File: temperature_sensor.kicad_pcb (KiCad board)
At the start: 2 copper layers, 8 parts, among them U3 XIAO-SAMD21-SMD, U4 AD589MH, U5 TMP37FT9Z

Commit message: i need to revert some of this to get my old stuff back lol
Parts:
- removed R10: 182k, Resistor_SMD:R_1210_3225Metric_Pad1.30x2.65mm_HandSolder
- removed R7: 45.3k, Resistor_SMD:R_1210_3225Metric_Pad1.30x2.65mm_HandSolder
- removed R8, R9: 10k, Resistor_SMD:R_1210_3225Metric_Pad1.30x2.65mm_HandSolder
- removed U4: AD589MH, 1_my_custom_library:AD589MH
- moved U5 25.7 mm to (68.3, 39.7)
- moved RF_interceptor1 17.4 mm to (66.9, 45.5)
- moved U3 5.62 mm to (45.0, 60.9)
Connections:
- U3 pad 2: unconnected-(U3-PA4_A1_D1-Pad2) -> Net-(U3-PA4_A1_D1)
- U5 pad 2: Net-(U5-VOUT) -> Net-(U3-PA4_A1_D1)
- U5 pad 3: Net-(U4-V-) -> GND

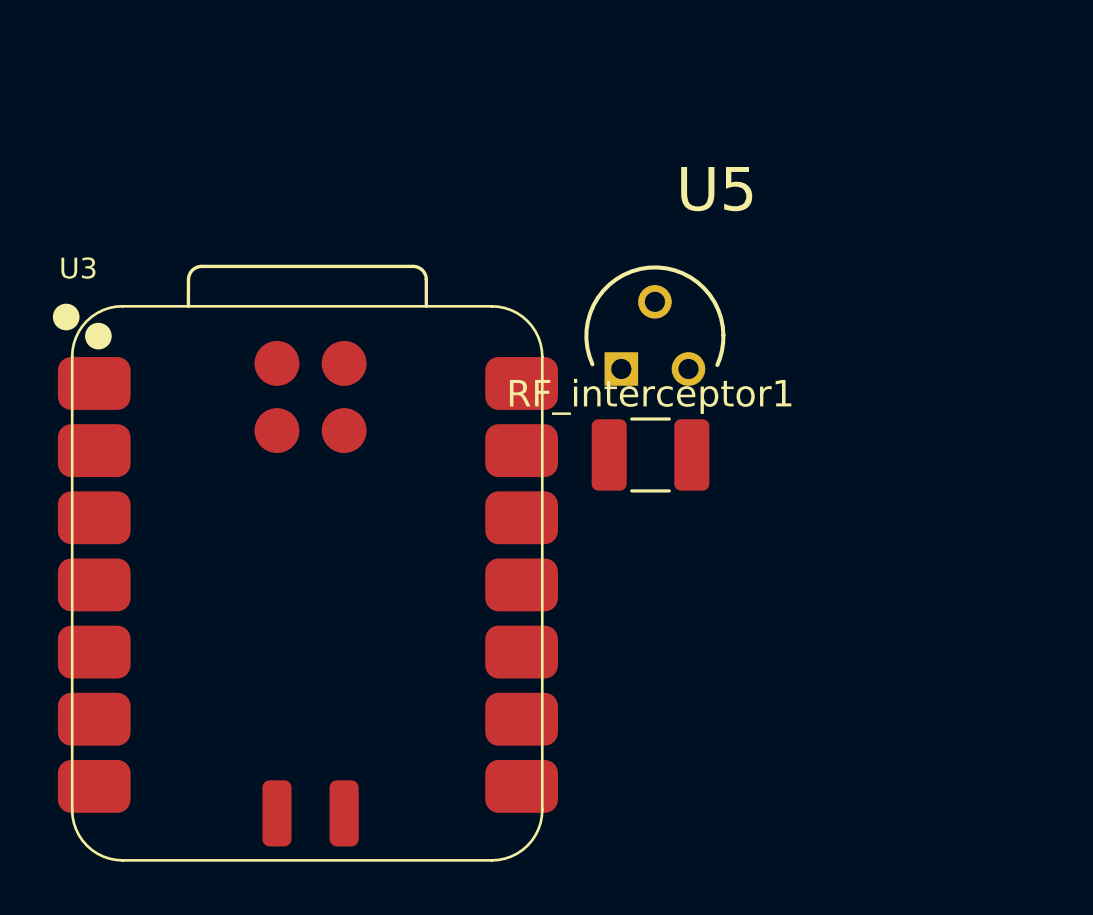
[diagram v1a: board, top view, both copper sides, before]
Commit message: added potentiometer, photoresistor, switch between the two and off, and added a F/C switch. need to up current into LCD's A pin
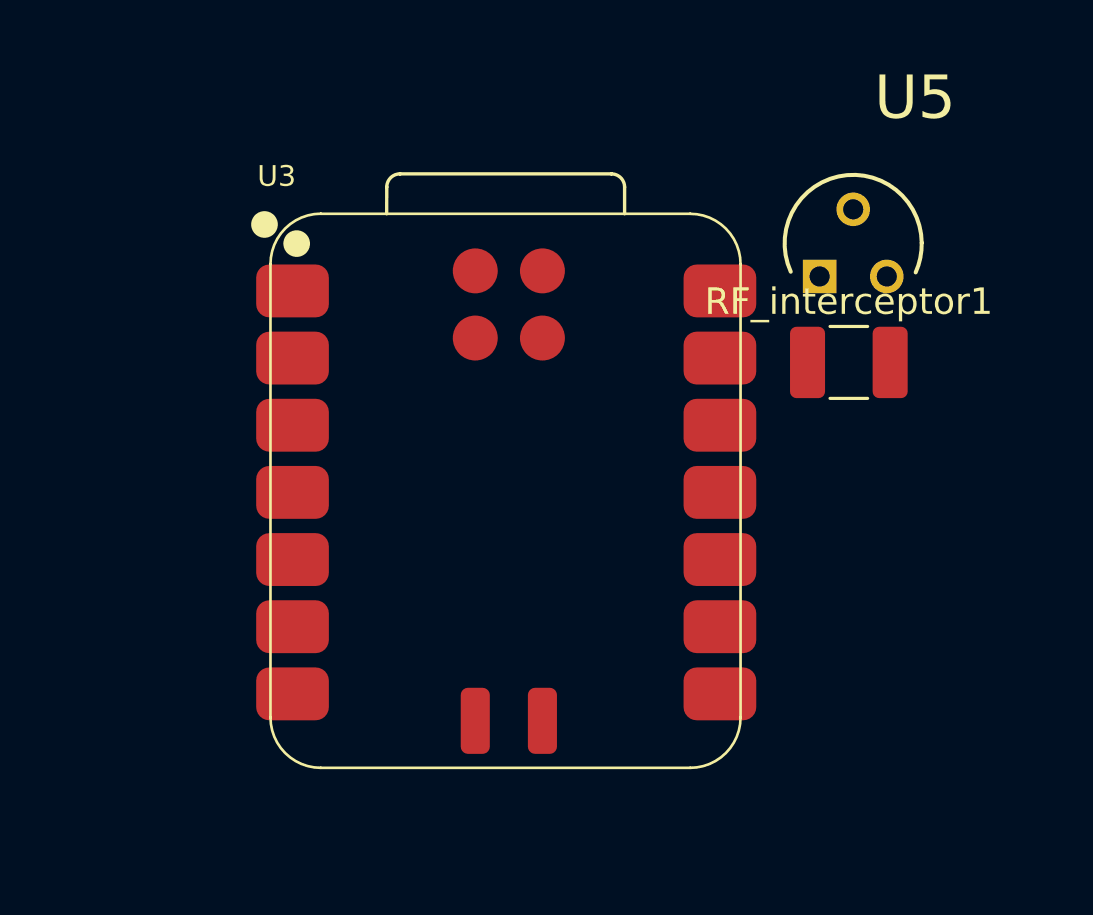
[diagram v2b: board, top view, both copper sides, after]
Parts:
- moved RF_interceptor1 8.28 mm to (74.4, 42.0)
- moved U3 8.28 mm to (52.5, 57.4)
- moved U5 8.28 mm to (75.8, 36.2)
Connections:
- net Net-(U3-3V3) renamed /3v3
- U3 pad 3: unconnected-(U3-PA10_A2_D2-Pad3) -> Net-(DS1-~{CS1})
- U3 pad 4: unconnected-(U3-PA11_A3_D3-Pad4) -> Net-(DS1-~{RES})
- U3 pad 5: unconnected-(U3-PA8_A4_D4_SDA-Pad5) -> Net-(DS1-A0)

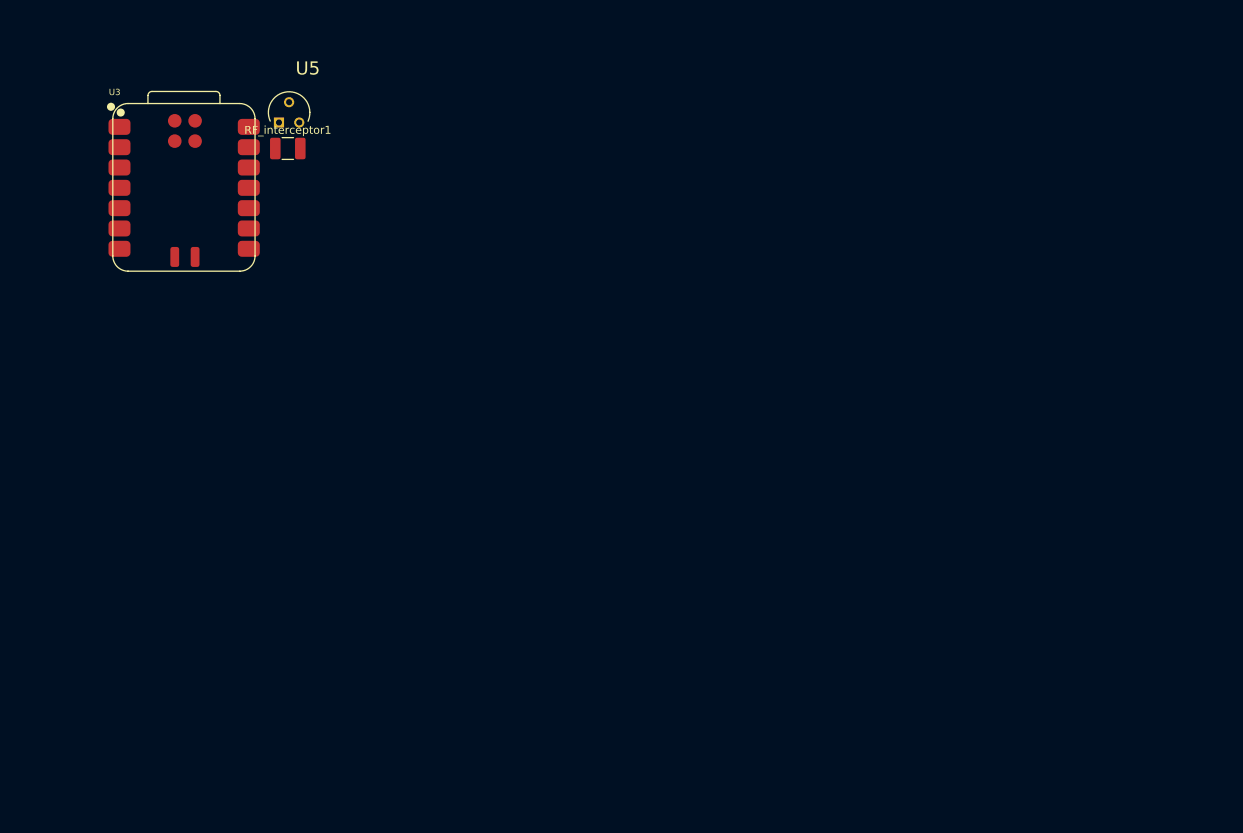
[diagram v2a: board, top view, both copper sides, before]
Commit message: got everything except the MOSFET to step up the current to 80mA.  all footprints added
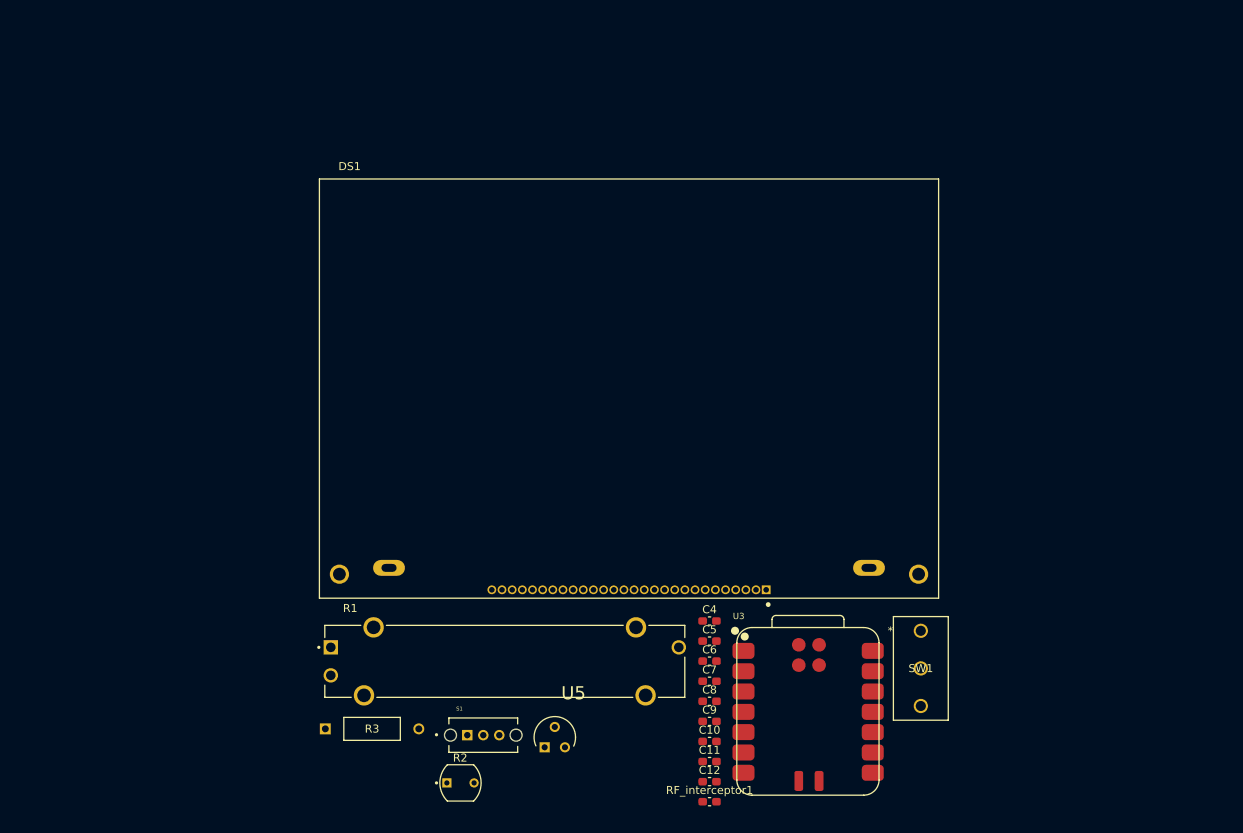
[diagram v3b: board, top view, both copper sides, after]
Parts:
- added C10: 1u, Capacitor_SMD:C_0603_1608Metric_Pad1.08x0.95mm_HandSolder, F.Cu at (127.1, 116.1)
- added C11: 1u, Capacitor_SMD:C_0603_1608Metric_Pad1.08x0.95mm_HandSolder, F.Cu at (127.1, 118.6)
- added C12: 1u, Capacitor_SMD:C_0603_1608Metric_Pad1.08x0.95mm_HandSolder, F.Cu at (127.1, 121.1)
- added C4: 2.2u, Capacitor_SMD:C_0603_1608Metric_Pad1.08x0.95mm_HandSolder, F.Cu at (127.1, 101.0)
- added C5: 2.2u, Capacitor_SMD:C_0603_1608Metric_Pad1.08x0.95mm_HandSolder, F.Cu at (127.1, 103.5)
- added C6: 2.2u, Capacitor_SMD:C_0603_1608Metric_Pad1.08x0.95mm_HandSolder, F.Cu at (127.1, 106.0)
- added C7: 2.2u, Capacitor_SMD:C_0603_1608Metric_Pad1.08x0.95mm_HandSolder, F.Cu at (127.1, 108.6)
- added C8: 2.2u, Capacitor_SMD:C_0603_1608Metric_Pad1.08x0.95mm_HandSolder, F.Cu at (127.1, 111.1)
- added C9: 1u, Capacitor_SMD:C_0603_1608Metric_Pad1.08x0.95mm_HandSolder, F.Cu at (127.1, 113.6)
- added DS1: NHD-C12864LZ-FSW-FBW-3V3, 1_my_custom_library:LCD_NHD-C12864LZ-FSW-FBW-3V3, F.Cu at (117.0, 98.2)
- added R1: PTA3043-2010CIB103, 1_my_custom_library:slide_potentiometer, F.Cu at (101.5, 106.1)
- added R2: PDV-P8103, 1_my_custom_library:photoresistor, F.Cu at (96.0, 121.3)
- added R3: 10k, 1_my_custom_library:YAG_MF25_YAG, F.Cu at (79.1, 114.5)
- added S1: OS102011MS2QN1, 1_my_custom_library:slideSwitch, F.Cu at (98.8, 115.3)
- added SW1: 500SSP3S1M2QEA, 1_my_custom_library:onOffOn, F.Cu at (153.5, 102.2)
- RF_interceptor1: footprint Capacitor_SMD:C_1210_3225Metric_Pad1.33x2.70mm_HandSolder -> Capacitor_SMD:C_0603_1608Metric_Pad1.08x0.95mm_HandSolder
- moved U3 101.9 mm to (130.5, 122.9)
- moved RF_interceptor1 97.2 mm to (127.1, 123.6)
- moved U5 84.9 mm to (109.0, 114.3)
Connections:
- net /3v3 renamed Net-(DS1-C86)
- U3 pad 1: unconnected-(U3-PA02_A0_D0-Pad1) -> Net-(U3-PA02_A0_D0)
- U3 pad 10: unconnected-(U3-PA5_A9_D9_MISO-Pad10) -> Net-(U3-PA5_A9_D9_MISO)
- U3 pad 13: unconnected-(U3-GND-Pad13) -> GND
- U3 pad 6: unconnected-(U3-PA9_A5_D5_SCL-Pad6) -> Net-(DS1-DB6)
- U3 pad 7: unconnected-(U3-PB08_A6_D6_TX-Pad7) -> Net-(DS1-A0)
- U3 pad 8: unconnected-(U3-PB09_A7_D7_RX-Pad8) -> Net-(DS1-~{WR}/R/W)
- U3 pad 9: unconnected-(U3-PA7_A8_D8_SCK-Pad9) -> Net-(U3-PA7_A8_D8_SCK)

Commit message: initial pcb design
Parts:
- added R4: 820, 1_my_custom_library:RESC6332X65N, F.Cu at (128.9, 87.5)
- added TP1: gnd_TP, Connector_Pin:Pin_D1.0mm_L10.0mm, F.Cu at (49.0, 112.0)
- added TP2: pot_TP, Connector_Pin:Pin_D1.0mm_L10.0mm, F.Cu at (63.0, 119.0)
- added TP3: photoresistor_TP, Connector_Pin:Pin_D1.0mm_L10.0mm, F.Cu at (63.0, 105.0)
- added TP4: PWM_TP, Connector_Pin:Pin_D1.0mm_L10.0mm, F.Cu at (56.0, 112.0)
- added TP5: K_TP, Connector_Pin:Pin_D1.0mm_L10.0mm, F.Cu at (63.0, 112.0)
- added TP6: SCL_TP, Connector_Pin:Pin_D1.0mm_L10.0mm, F.Cu at (56.0, 119.0)
- added TP7: SI_TP, Connector_Pin:Pin_D1.0mm_L10.0mm, F.Cu at (49.0, 119.0)
- added TP8: fahrenheit_celsius_TP, Connector_Pin:Pin_D1.0mm_L10.0mm, F.Cu at (56.0, 105.0)
- added TP9: 3v3_TP, Connector_Pin:Pin_D1.0mm_L10.0mm, F.Cu at (49.0, 105.0)
- added U1: MMBT3904LT1G, 1_my_custom_library:SOT-23_3L_ONS, F.Cu at (114.0, 87.0)
- moved U5 110.6 mm to (177.5, 27.5)
- moved R2 110.4 mm to (155.8, 28.5), turned to 180 degrees
- moved R3 104.1 mm to (150.2, 38.5)
- moved RF_interceptor1 98.8 mm to (176.3, 38.0), turned to 180 degrees
- moved S1 91.8 mm to (177.5, 68.0)
- moved C6 73.3 mm to (55.5, 90.5), turned to 90 degrees
- moved C5 69.8 mm to (58.5, 90.5), turned to 90 degrees
- moved C4 65.9 mm to (62.0, 90.5), turned to 90 degrees
- moved C8 64.9 mm to (65.5, 90.5), turned to 90 degrees
- moved C7 62.7 mm to (65.9, 95.0)
- moved R1 61.6 mm to (136.0, 55.0), turned to 90 degrees
- moved C10 61.6 mm to (71.0, 90.6), turned to 90 degrees
- moved C12 61.2 mm to (74.0, 90.6), turned to 90 degrees
- moved C11 56.9 mm to (77.5, 90.6), turned to 90 degrees
- moved U3 54.3 mm to (169.2, 84.8), turned to -90 degrees
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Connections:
- DS1 pad A: Net-(U3-PA02_A0_D0) -> Net-(DS1-C86)
- DS1 pad K: GND -> Net-(U1-COLLECTOR)
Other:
- board outline added: 150 x 100 mm

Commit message: sent for prod v1.0
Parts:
- added G***: LOGO, LOGO, B.Cu at (175.5, 107.0)
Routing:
- net GND: track 0.00 -> 597.0 mm
- net Net-(DS1-C86): track 0.00 -> 385.0 mm
- net /bc1: track 0.00 -> 260.6 mm, vias 0 -> 2
- net Net-(DS1-DB6): track 0.00 -> 223.1 mm, vias 0 -> 5
- net Net-(DS1-DB7): track 0.00 -> 210.3 mm, vias 0 -> 3
- net /bc2: track 0.00 -> 195.1 mm, vias 0 -> 6
- net Net-(U3-PA7_A8_D8_SCK): track 0.00 -> 169.2 mm, vias 0 -> 2
- net Net-(DS1-~{RES}): track 0.00 -> 143.0 mm, vias 0 -> 1
- net Net-(DS1-A0): track 0.00 -> 129.4 mm, vias 0 -> 3
- net Net-(U1-BASE): track 0.00 -> 100.0 mm, vias 0 -> 3
- net Net-(DS1-~{CS1}): track 0.00 -> 90.6 mm, vias 0 -> 1
- net Net-(DS1-~{WR}/R/W): track 0.00 -> 87.2 mm, vias 0 -> 1
- net (no net): track 0.00 -> 84.2 mm, vias 0 -> 2
- net Net-(U3-PA02_A0_D0): track 0.00 -> 83.7 mm, vias 0 -> 2
- net Net-(U1-COLLECTOR): track 0.00 -> 70.5 mm, vias 0 -> 1
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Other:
- outline, holes or cut-outs redrawn
- board text added: "3v3 F/C photores GND PWM backlight(-) sda sclk slide pot"
- board text added: "A0(O1): LCD PWM A1(I2): Temperature A2(O3): LCD ~CS A3(O4): LCD ~RESET A4(O5): LCD Serial data A5(O6): LCD Serial clock A6(O7): LCD A0 A7(O8): LCD R/W=1:Read R/W=0:Write A8(I9): Fahrenheit/Celsius toggle switch A9(I10): LCD backlight brightness source A10(X11): No connect P(O12): 3V3 P(O13): GND P(O14): 5V P(I15): Vin P(I16): GND X(X17): No connect X(X18): No connect X(X19): RESET - No connect P(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"
- board text added: "SAMD21 Pins:"
- board text added: "Temperature Monitor v1.0 Logan Slowik"
- board text added: "Test points"
